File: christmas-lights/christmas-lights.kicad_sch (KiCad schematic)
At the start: 1 part, among them U1 ESP-12E

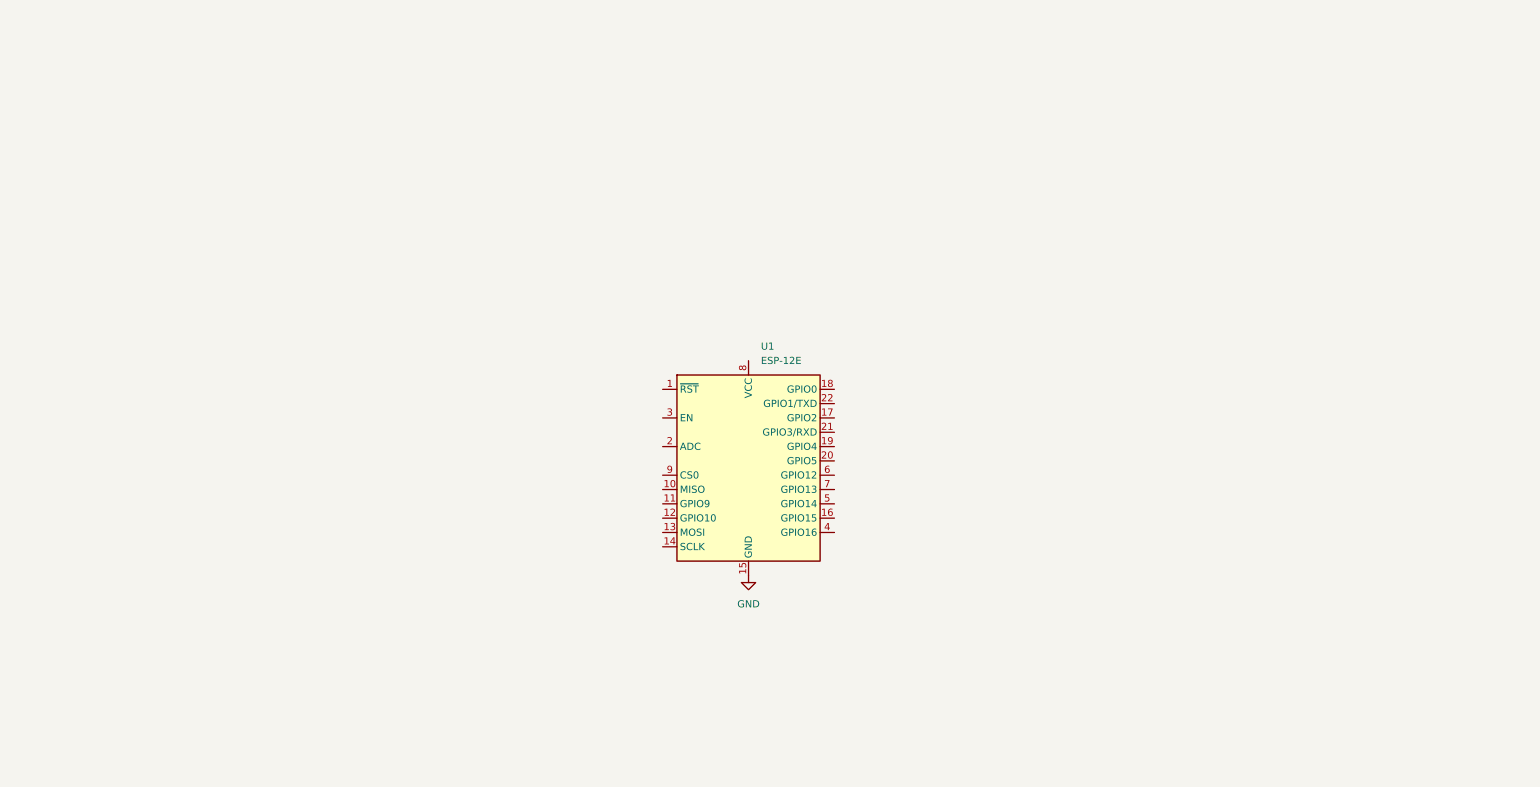
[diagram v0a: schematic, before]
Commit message: Added 3.3V DC Regulator Power Supply
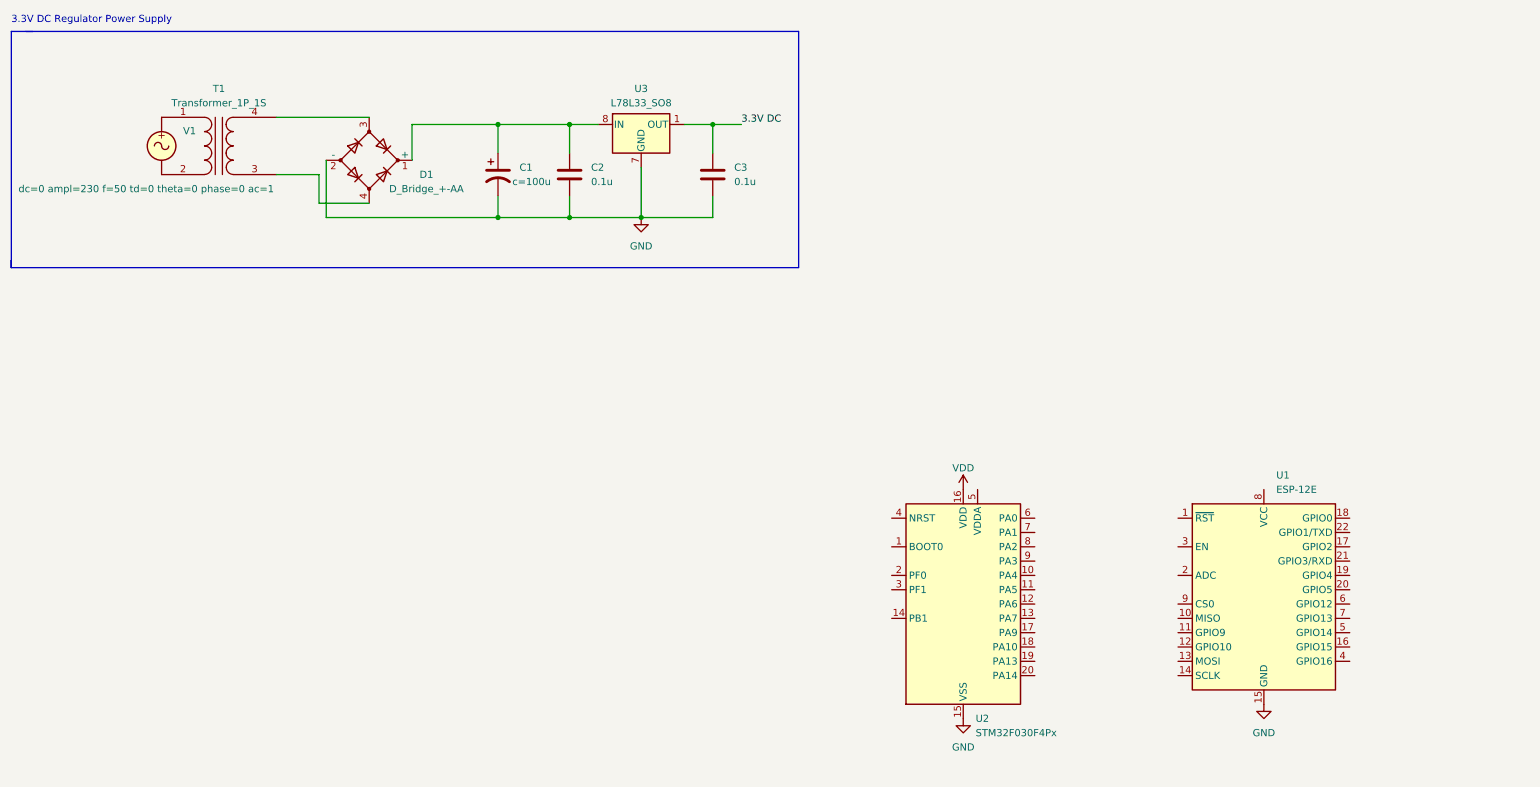
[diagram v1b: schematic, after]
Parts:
- added C1: ${SIM.PARAMS}, symbol Device:C_Polarized_US
- added C2, C3: 0.1u, symbol Device:C
- added D1: D_Bridge_+-AA, symbol Device:D_Bridge_+-AA
- added T1: Transformer_1P_1S, symbol Device:Transformer_1P_1S
- added U2: STM32F030F4Px, Package_SO:TSSOP-20_4.4x6.5mm_P0.65mm, symbol MCU_ST_STM32F0:STM32F030F4Px
- added U3: L78L33_SO8, Package_SO:SOIC-8_3.9x4.9mm_P1.27mm, symbol Regulator_Linear:L78L33_SO8
- added V1: ~, symbol Simulation_SPICE:VSIN
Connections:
- net GND: now also C1.2, C2.2, C3.2, D1.2 (-), U2.15 (VSS), U3.2 (GND), U3.3 (GND), U3.6 (GND), U3.7 (GND)
- new net: C1.1, C2.1, D1.1 (+), U3.8 (IN)
- new net: T1.1 (AA), V1.1
- new net: T1.2 (AB), V1.2
- new net: D1.4, T1.3 (SA)
- new net: D1.3, T1.4 (SB)
- new net 3.3V DC: C3.1, U3.1 (OUT)
- new net VDD: U2.16 (VDD)
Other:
- note added: "3.3V DC Regulator Power Supply"
- moved on the sheet: U1

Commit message: Schematic
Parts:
- removed C1: ${SIM.PARAMS}, symbol Device:C_Polarized_US
- removed C2, C3: 0.1u, symbol Device:C
- removed D1: D_Bridge_+-AA, symbol Device:D_Bridge_+-AA
- removed T1: Transformer_1P_1S, symbol Device:Transformer_1P_1S
- removed U2: STM32F030F4Px, Package_SO:TSSOP-20_4.4x6.5mm_P0.65mm, symbol MCU_ST_STM32F0:STM32F030F4Px
- removed U3: L78L33_SO8, Package_SO:SOIC-8_3.9x4.9mm_P1.27mm, symbol Regulator_Linear:L78L33_SO8
- removed V1: ~, symbol Simulation_SPICE:VSIN
- added C1: 1uF, symbol Device:C_Small
- added C2: 4.7uF, symbol Device:C_Small
- added C3: 100nF, symbol Device:C_Small
- added C4, C5: 10uF, symbol Device:C_Small
- added J1: Barrel_Jack_Switch, symbol Connector:Barrel_Jack_Switch
- added J2: Conn_01x04, symbol Connector_Generic:Conn_01x04
- added Q1, Q2, Q3: NMOS, symbol Simulation_SPICE:NMOS
- added R1, R2, R3, R4, R5: 10k, symbol Device:R_Small
- added U2: SPX3819M5-L-3-3, Package_TO_SOT_SMD:SOT-23-5, symbol Regulator_Linear:SPX3819M5-L-3-3
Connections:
- net GND: now also C1.2, C2.2, C3.2, C4.2, C5.2, J1.2, Q1.3 (S), Q2.3 (S), Q3.3 (S), R3.1, U2.2 (GND)
- net VDD: now also U1.8 (VCC), C1.1, C2.1, C4.1, R1.1, R2.1, R4.2, R5.2, U2.5 (OUT)
- net at U1.1 (~{RST}): now also C3.1, R2.2
- net at U1.16 (GPIO15): now also R3.2
- net at U1.17 (GPIO2): now also R5.1
- net at U1.18 (GPIO0): now also R4.1
- net at U1.3 (EN): now also R1.2
- net BMOS: now reaches U1.5 (GPIO14)
- net BMOS: now also Q3.2 (G)
- net RMOS: now reaches U1.6 (GPIO12)
- net RMOS: now also Q1.2 (G)
- net GMOS: now reaches U1.7 (GPIO13)
- net GMOS: now also Q2.2 (G)
- new net: J2.2 (Pin_2), Q1.1 (D)
- new net: J2.3 (Pin_3), Q2.1 (D)
- new net: J2.4 (Pin_4), Q3.1 (D)
- new net +12V: J1.1, J2.1 (Pin_1)
- new net +5V: C5.1, U2.1 (IN), U2.3 (EN)
- no-connect marks 0 -> 14
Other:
- note added: "For ERC only"
- note added: "MCU"
- note added: "PSU"
- note removed: "3.3V DC Regulator Power Supply"
- title: (none) -> Christmas lights

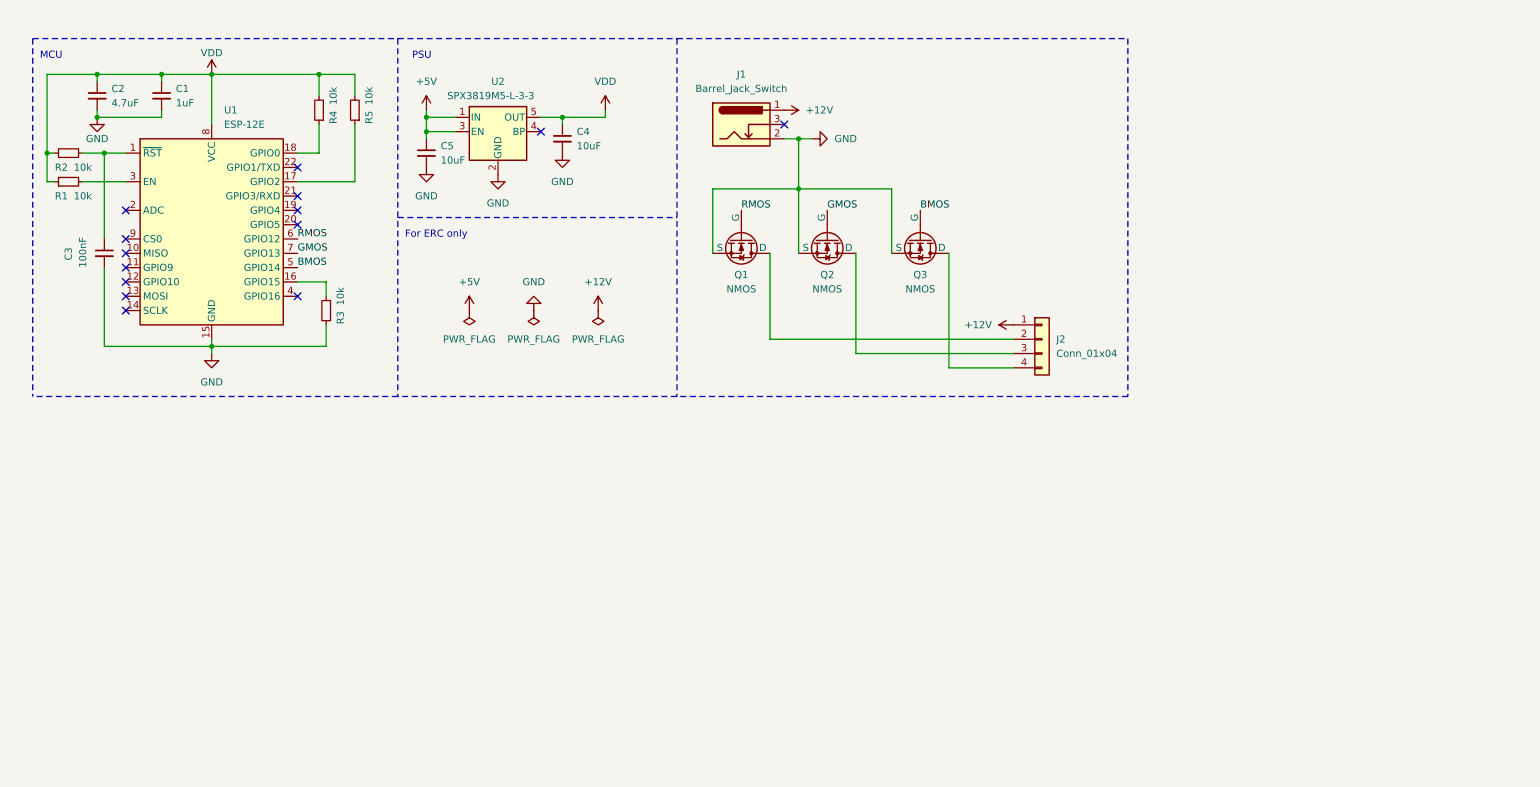
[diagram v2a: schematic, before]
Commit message: Added USB to UART interface
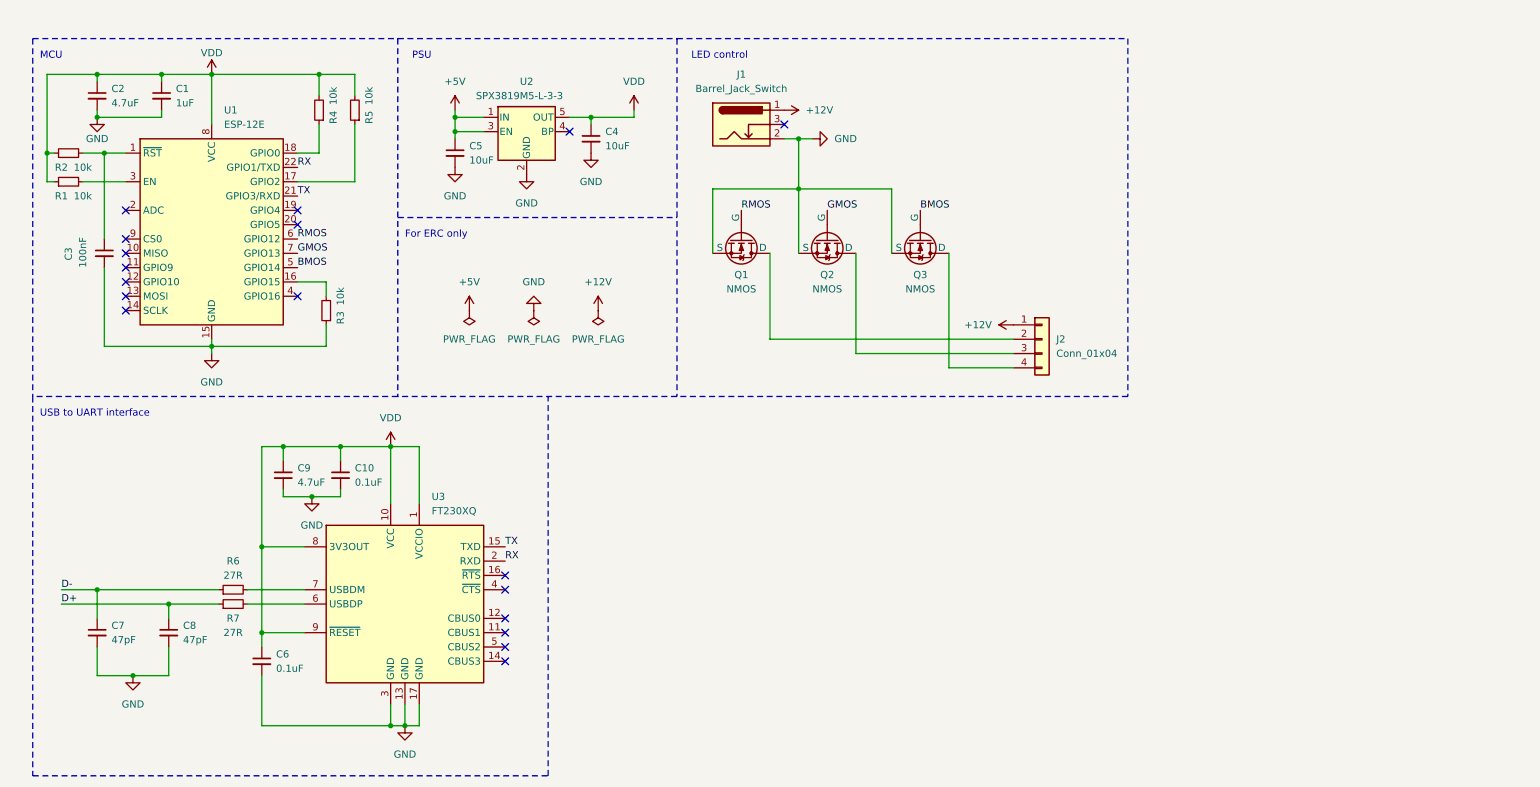
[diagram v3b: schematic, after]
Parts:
- added C10, C6: 0.1uF, symbol Device:C_Small
- added C7, C8: 47pF, symbol Device:C_Small
- added C9: 4.7uF, symbol Device:C_Small
- added R6, R7: 27R, symbol Device:R_Small
- added U3: FT230XQ, Package_DFN_QFN:QFN-16-1EP_4x4mm_P0.65mm_EP2.1x2.1mm, symbol Interface_USB:FT230XQ
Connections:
- net GND: now also C10.2, C6.2, C7.2, C8.2, C9.2, U3.13 (GND), U3.17 (GND), U3.3 (GND)
- net VDD: now also C10.1, C6.1, C9.1, U3.1 (VCCIO), U3.10 (VCC), U3.8 (3V3OUT), U3.9 (~{RESET})
- net TX: now reaches U1.21 (GPIO3/RXD)
- net TX: now also U3.15 (TXD)
- net RX: now reaches U1.22 (GPIO1/TXD)
- net RX: now also U3.2 (RXD)
- new net: R6.2, U3.7 (USBDM)
- new net: R7.2, U3.6 (USBDP)
- new net D+: C8.1, R7.1
- new net D-: C7.1, R6.1
- no-connect marks 14 -> 18
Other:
- note added: "LED control"
- note added: "USB to UART interface"
- moved on the sheet: C4, C5, U2

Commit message: Added port expander etc.
Added:
-port expander
-reset switch
-USB connector
-more LED strips to the control circuit
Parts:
- removed J1: Barrel_Jack_Switch, symbol Connector:Barrel_Jack_Switch
- removed J2: Conn_01x04, symbol Connector_Generic:Conn_01x04
- removed Q1, Q2, Q3: NMOS, symbol Simulation_SPICE:NMOS
- added C11: 0.1uF, symbol Device:C_Small
- added J3: Conn_01x06, symbol Connector_Generic:Conn_01x06
- added J5: Barrel_Jack_Switch, symbol Connector:Barrel_Jack_Switch
- added J6: USB_A, symbol Connector:USB_A
- added J7: Conn_01x10, symbol Connector_Generic:Conn_01x10
- added Q10, Q11, Q12, Q4, Q5, Q6, Q7, Q8, Q9: NMOS, symbol Simulation_SPICE:NMOS
- added R10: 10k, symbol Device:R_Small
- added R8, R9: 1k tbd, symbol Device:R_Small
- added SW1: SW_MEC_5G, symbol Switch:SW_MEC_5G
- added U4: MCP23008-xP, Package_DIP:DIP-18_W7.62mm, symbol Interface_Expansion:MCP23008-xP
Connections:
- net +12V: now also J5.1, J7.1 (Pin_1)
- net +5V: now also C11.2, J6.1 (VBUS), R8.1, R9.1, U4.18 (VDD)
- net D+: now also J6.3 (D+)
- net D-: now also J6.2 (D-)
- net GND: now also R2.1, C11.1, J5.2, J6.4 (GND), J6.5 (Shield), Q10.3 (S), Q11.3 (S), Q12.3 (S), Q4.3 (S), Q5.3 (S), Q6.3 (S), Q7.3 (S), Q8.3 (S), Q9.3 (S), SW1.3 (B), SW1.4 (B), U4.9 (VSS)
- net VDD: now also C3.1, R2.2, R10.1; no longer C6.1, R2.1, U3.8 (3V3OUT), U3.9 (~{RESET})
- net SDA: now reaches U1.19 (GPIO4)
- net SDA: now also R9.2, U4.2 (SDA)
- net SCL: now reaches U1.20 (GPIO5)
- net SCL: now also R8.2, U4.1 (SCL)
- net BMOS renamed BLUE1
- net BLUE1: now also Q6.2 (G)
- net GMOS renamed GREEN1
- net GREEN1: now also Q5.2 (G)
- net RMOS renamed RED1
- net RED1: now also Q4.2 (G)
- new net: J7.5 (Pin_5), Q7.1 (D)
- new net: J7.10 (Pin_10), Q12.1 (D)
- new net: J7.8 (Pin_8), Q10.1 (D)
- new net: C6.1, U3.8 (3V3OUT), U3.9 (~{RESET})
- new net: J7.7 (Pin_7), Q9.1 (D)
- new net: J7.3 (Pin_3), Q5.1 (D)
- new net: J7.4 (Pin_4), Q6.1 (D)
- new net: J7.2 (Pin_2), Q4.1 (D)
- new net: J7.6 (Pin_6), Q8.1 (D)
- new net: J7.9 (Pin_9), Q11.1 (D)
- new net BLUE2: J3.4 (Pin_4), Q9.2 (G), U4.12 (GP2)
- new net BLUE3: J3.1 (Pin_1), Q12.2 (G), U4.15 (GP5)
- new net GREEN2: J3.5 (Pin_5), Q8.2 (G), U4.11 (GP1)
- new net GREEN3: J3.2 (Pin_2), Q11.2 (G), U4.14 (GP4)
- new net RED2: J3.6 (Pin_6), Q7.2 (G), U4.10 (GP0)
- new net RED3: J3.3 (Pin_3), Q10.2 (G), U4.13 (GP3)
- new net RST: R10.2, SW1.1 (A), SW1.2 (A), U1.1 (~{RST}), U4.6 (~{RESET})
- no-connect marks 18 -> 22
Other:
- note added: "I/O expander"
- note added: "Reset switch"
- note added: "USB connector"
- moved on the sheet: R2
